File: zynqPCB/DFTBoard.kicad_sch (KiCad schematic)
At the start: 0 parts

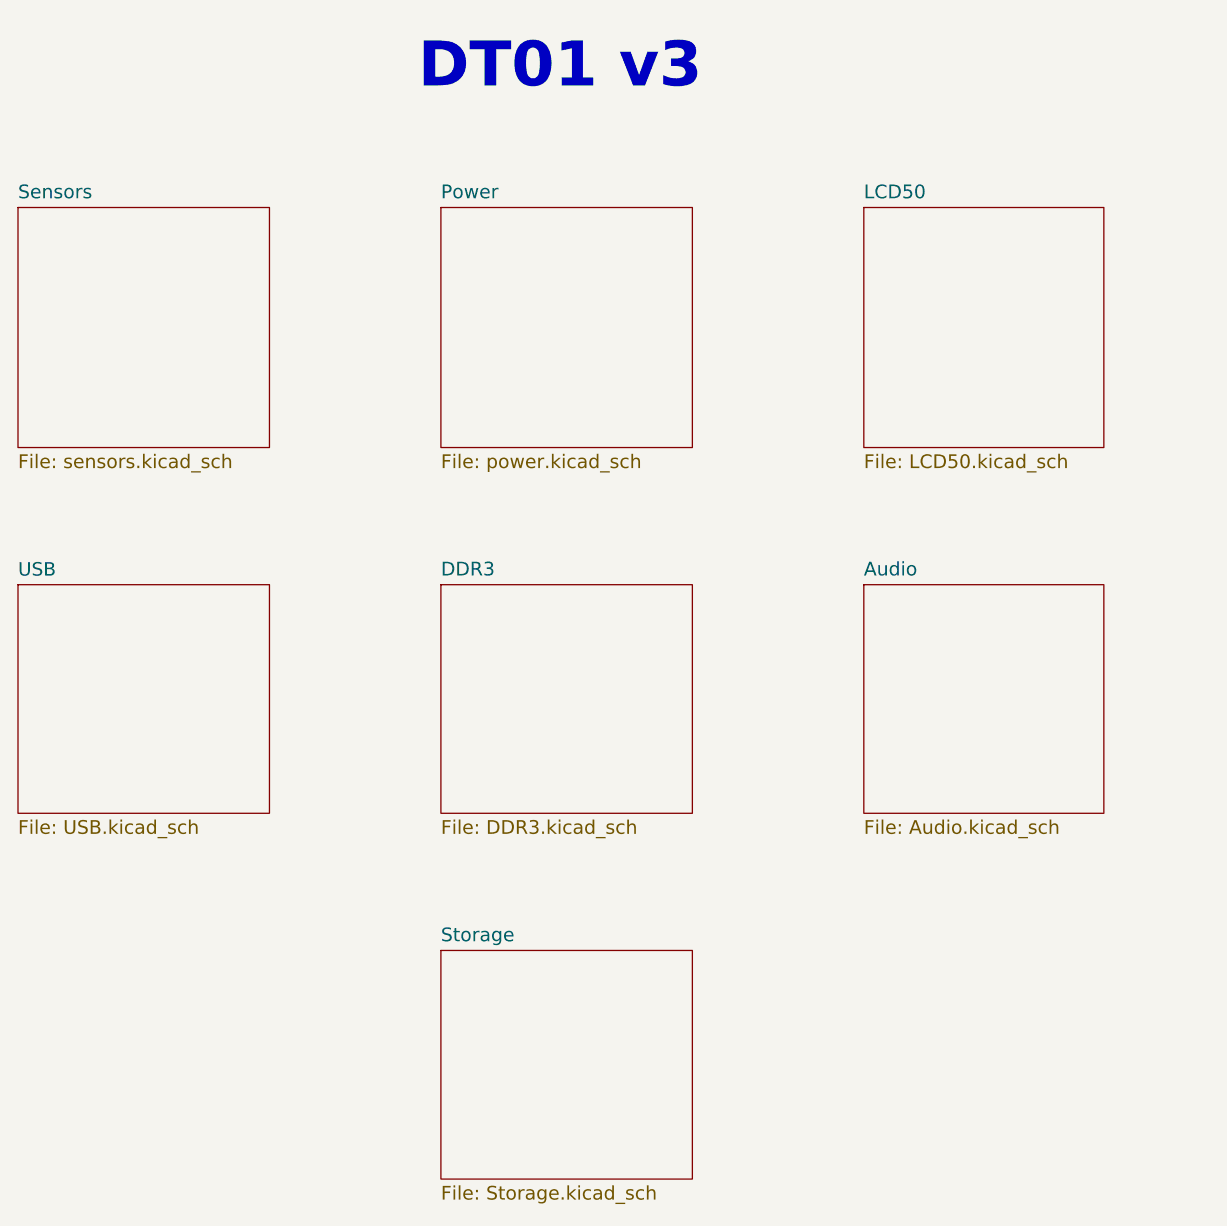
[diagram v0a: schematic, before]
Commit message: Sensores Removed
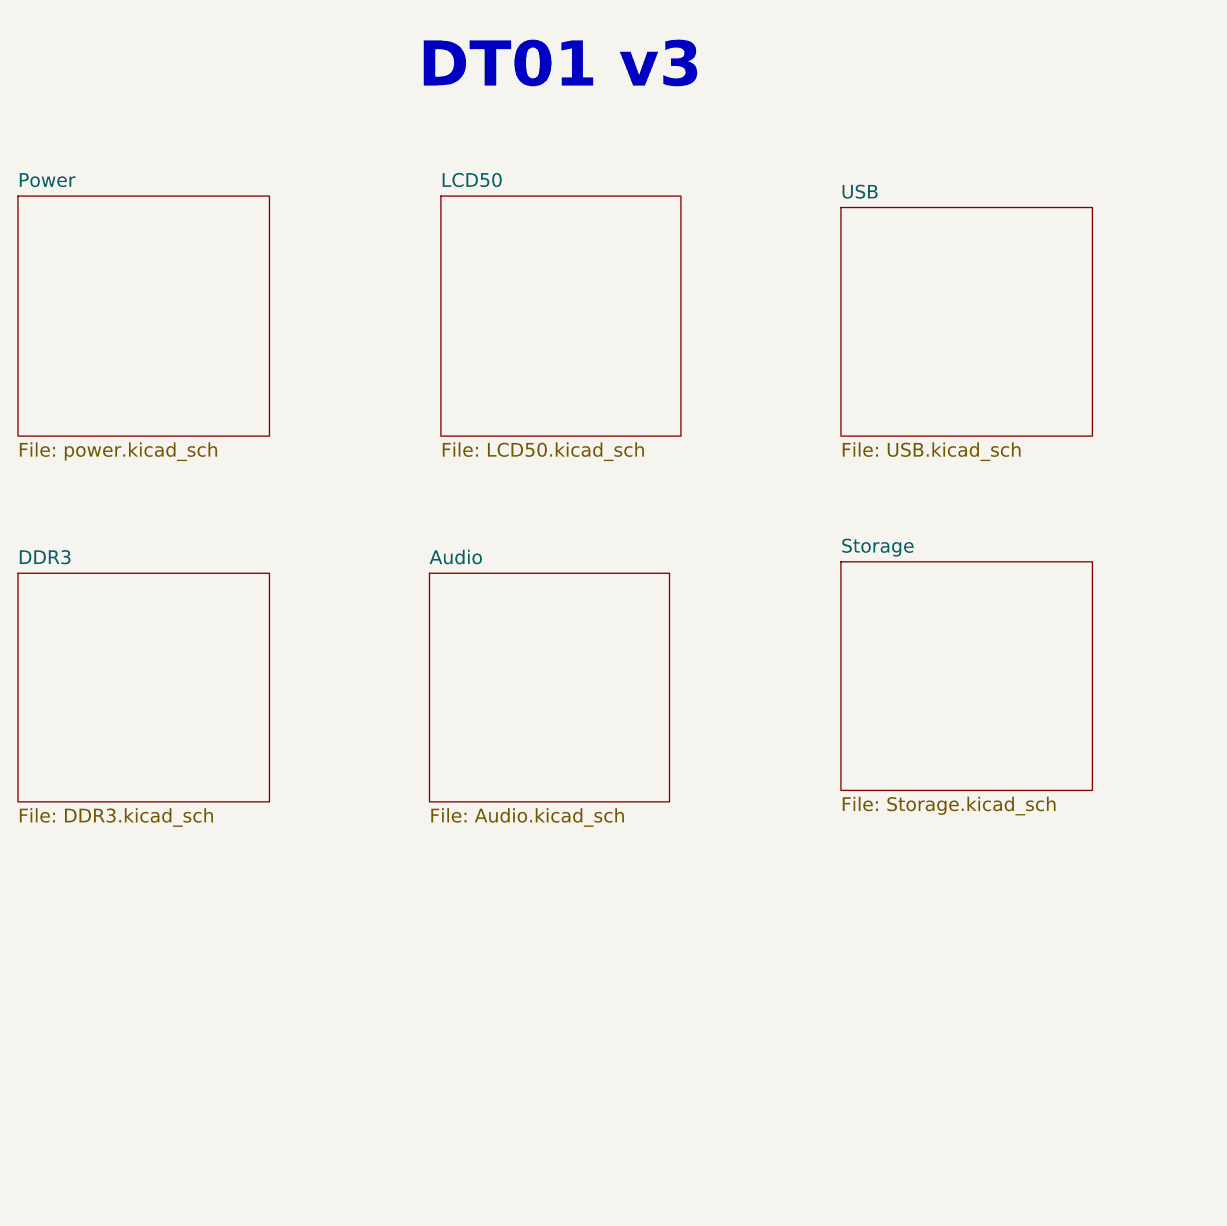
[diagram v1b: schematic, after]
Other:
- removed sheet Sensors
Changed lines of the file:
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@@
 	)
 	(sheet
-		(at 137.16 52.07)
+		(at 90.17 50.8)
 		(size 27.94 26.67)
 		(exclude_from_sim no)
@@
 		)
 		(property "Sheetname" "Power"
-			(at 137.16 51.2314 0)
+			(at 90.17 49.9614 0)
 			(effects
 				(font
@@
 		)
 		(property "Sheetfile" "power.kicad_sch"
-			(at 137.16 79.4262 0)
+			(at 90.17 78.1562 0)
 			(effects
 				(font
@@
 	)
 	(sheet
-		(at 184.15 93.98)
+		(at 135.89 92.71)
 		(size 26.67 25.4)
 		(exclude_from_sim no)
@@
 		)
 		(property "Sheetname" "Audio"
-			(at 184.15 93.1414 0)
+			(at 135.89 91.8714 0)
 			(effects
 				(font
@@
 		)
 		(property "Sheetfile" "Audio.kicad_sch"
-			(at 184.15 120.0662 0)
+			(at 135.89 118.7962 0)
 			(effects
 				(font
@@
 	)
 	(sheet
-		(at 90.17 93.98)
+		(at 181.61 52.07)
 		(size 27.94 25.4)
 		(exclude_from_sim no)
@@
 		)
 		(property "Sheetname" "USB"
-			(at 90.17 93.1541 0)
+			(at 181.61 51.2441 0)
 			(effects
 				(font
@@
 		)
 		(property "Sheetfile" "USB.kicad_sch"
-			(at 90.17 120.0662 0)
+			(at 181.61 78.1562 0)
 			(effects
 				(font
@@
 	)
 	(sheet
-		(at 90.17 52.07)
-		(size 27.94 26.67)
-		(exclude_from_sim no)
-		(in_bom yes)
-		(on_board yes)
-		(dnp no)
-		(fields_autoplaced yes)
-		(stroke
-			(width 0)
-			(type solid)
-		)
-		(fill
-			(color 0 0 0 0.0000)
-		)
-		(property "Sheetname" "Sensors"
-			(at 90.17 51.2314 0)
-			(effects
-				(font
-					(size 1.524 1.524)
-				)
-				(justify left bottom)
-			)
-		)
-		(property "Sheetfile" "sensors.kicad_sch"
-			(at 90.17 79.4262 0)
-			(effects
-				(font
-					(size 1.524 1.524)
-				)
-				(justify left top)
-			)
-		)
-		(instances
-			(project "DFTBoard"
-				(path "/49eba173-d38c-4d05-b21c-b4a14c4948c2"
-					(page "2")
-				)
-			)
-		)
-	)
-	(sheet
-		(at 137.16 93.98)
+		(at 90.17 92.71)
 		(size 27.94 25.4)
 		(exclude_from_sim no)
@@
 		)
 		(property "Sheetname" "DDR3"
-			(at 137.16 93.1414 0)
+			(at 90.17 91.8714 0)
 			(effects
 				(font
@@
 		)
 		(property "Sheetfile" "DDR3.kicad_sch"
-			(at 137.16 120.0662 0)
+			(at 90.17 118.7962 0)
 			(effects
 				(font
@@
 	)
 	(sheet
-		(at 184.15 52.07)
+		(at 137.16 50.8)
 		(size 26.67 26.67)
 		(exclude_from_sim no)
@@
 		)
 		(property "Sheetname" "LCD50"
-			(at 184.15 51.2314 0)
+			(at 137.16 49.9614 0)
 			(effects
 				(font
@@
 		)
 		(property "Sheetfile" "LCD50.kicad_sch"
-			(at 184.15 79.4262 0)
+			(at 137.16 78.1562 0)
 			(effects
 				(font
@@
 	)
 	(sheet
-		(at 137.16 134.62)
+		(at 181.61 91.44)
 		(size 27.94 25.4)
 		(exclude_from_sim no)
@@
 		)
 		(property "Sheetname" "Storage"
-			(at 137.16 133.7814 0)
+			(at 181.61 90.6014 0)
 			(effects
 				(font
@@
 		)
 		(property "Sheetfile" "Storage.kicad_sch"
-			(at 137.16 160.7062 0)
-			(effects
-				(font
+			(at 181.61 117.5262 0)
+			(effects
+				(font

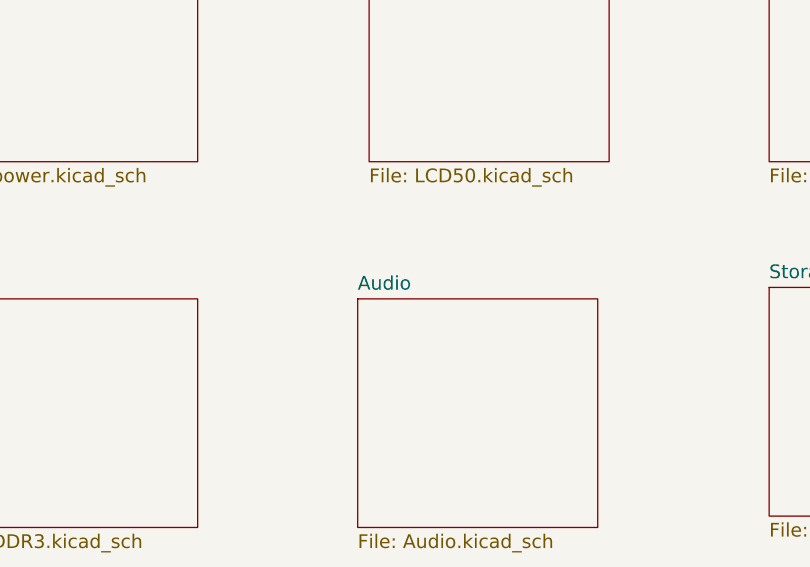
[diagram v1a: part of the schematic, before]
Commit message: Camera added
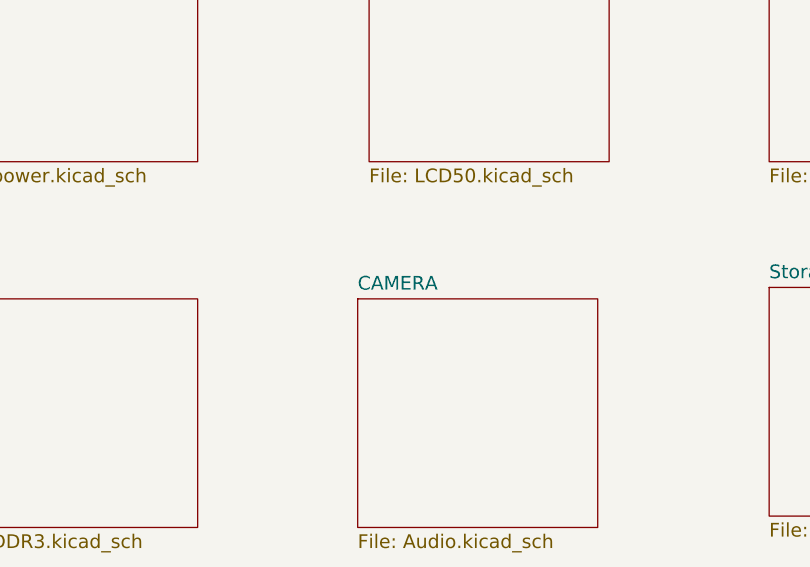
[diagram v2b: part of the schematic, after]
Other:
- sheet Audio renamed CAMERA
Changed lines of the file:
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@@
 (kicad_sch
-	(version 20250114)
+	(version 20260306)
 	(generator "eeschema")
-	(generator_version "9.0")
+	(generator_version "10.0")
 	(paper "A4")
 	(text "DT01 v3"
@@
 		)
 		(fill
-			(color 0 0 0 0.0000)
+			(color 0 0 0 0)
 		)
 		(property "Sheetname" "Power"
 			(at 90.17 49.9614 0)
+			(show_name no)
+			(do_not_autoplace no)
 			(effects
 				(font
@@
 		(property "Sheetfile" "power.kicad_sch"
 			(at 90.17 78.1562 0)
+			(show_name no)
+			(do_not_autoplace no)
 			(effects
 				(font
@@
 		)
 		(fill
-			(color 0 0 0 0.0000)
-		)
-		(property "Sheetname" "Audio"
+			(color 0 0 0 0)
+		)
+		(property "Sheetname" "CAMERA"
 			(at 135.89 91.8714 0)
+			(show_name no)
+			(do_not_autoplace no)
 			(effects
 				(font
@@
 		(property "Sheetfile" "Audio.kicad_sch"
 			(at 135.89 118.7962 0)
+			(show_name no)
+			(do_not_autoplace no)
 			(effects
 				(font
@@
 		)
 		(fill
-			(color 0 0 0 0.0000)
+			(color 0 0 0 0)
 		)
 		(property "Sheetname" "USB"
 			(at 181.61 51.2441 0)
+			(show_name no)
+			(do_not_autoplace no)
 			(effects
 				(font
@@
 		(property "Sheetfile" "USB.kicad_sch"
 			(at 181.61 78.1562 0)
+			(show_name no)
+			(do_not_autoplace no)
 			(effects
 				(font
@@
 		)
 		(fill
-			(color 0 0 0 0.0000)
+			(color 0 0 0 0)
 		)
 		(property "Sheetname" "DDR3"
 			(at 90.17 91.8714 0)
+			(show_name no)
+			(do_not_autoplace no)
 			(effects
 				(font
@@
 		(property "Sheetfile" "DDR3.kicad_sch"
 			(at 90.17 118.7962 0)
+			(show_name no)
+			(do_not_autoplace no)
 			(effects
 				(font
@@
 		)
 		(fill
-			(color 0 0 0 0.0000)
+			(color 0 0 0 0)
 		)
 		(property "Sheetname" "LCD50"
 			(at 137.16 49.9614 0)
+			(show_name no)
+			(do_not_autoplace no)
 			(effects
 				(font
@@
 		(property "Sheetfile" "LCD50.kicad_sch"
 			(at 137.16 78.1562 0)
+			(show_name no)
+			(do_not_autoplace no)
 			(effects
 				(font
@@
 		)
 		(fill
-			(color 0 0 0 0.0000)
+			(color 0 0 0 0)
 		)
 		(property "Sheetname" "Storage"
 			(at 181.61 90.6014 0)
+			(show_name no)
+			(do_not_autoplace no)
 			(effects
 				(font
@@
 		(property "Sheetfile" "Storage.kicad_sch"
 			(at 181.61 117.5262 0)
-			(effects
-				(font
+			(show_name no)
+			(do_not_autoplace no)
+			(effects
+				(font

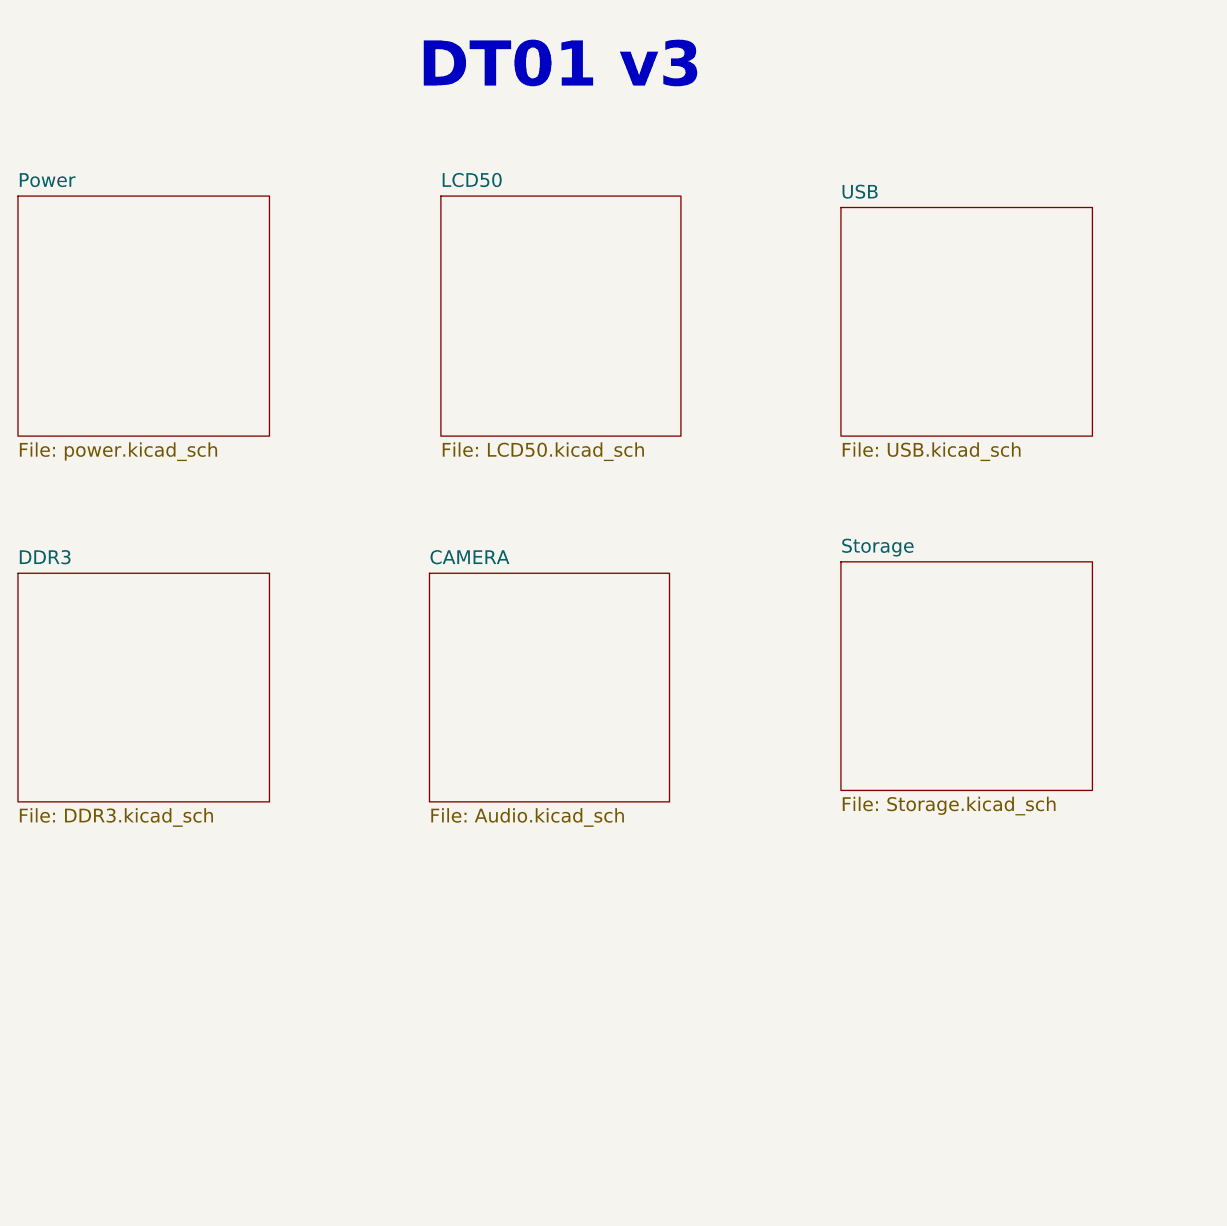
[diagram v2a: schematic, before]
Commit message: Cleared ERC error except the sequencer Part
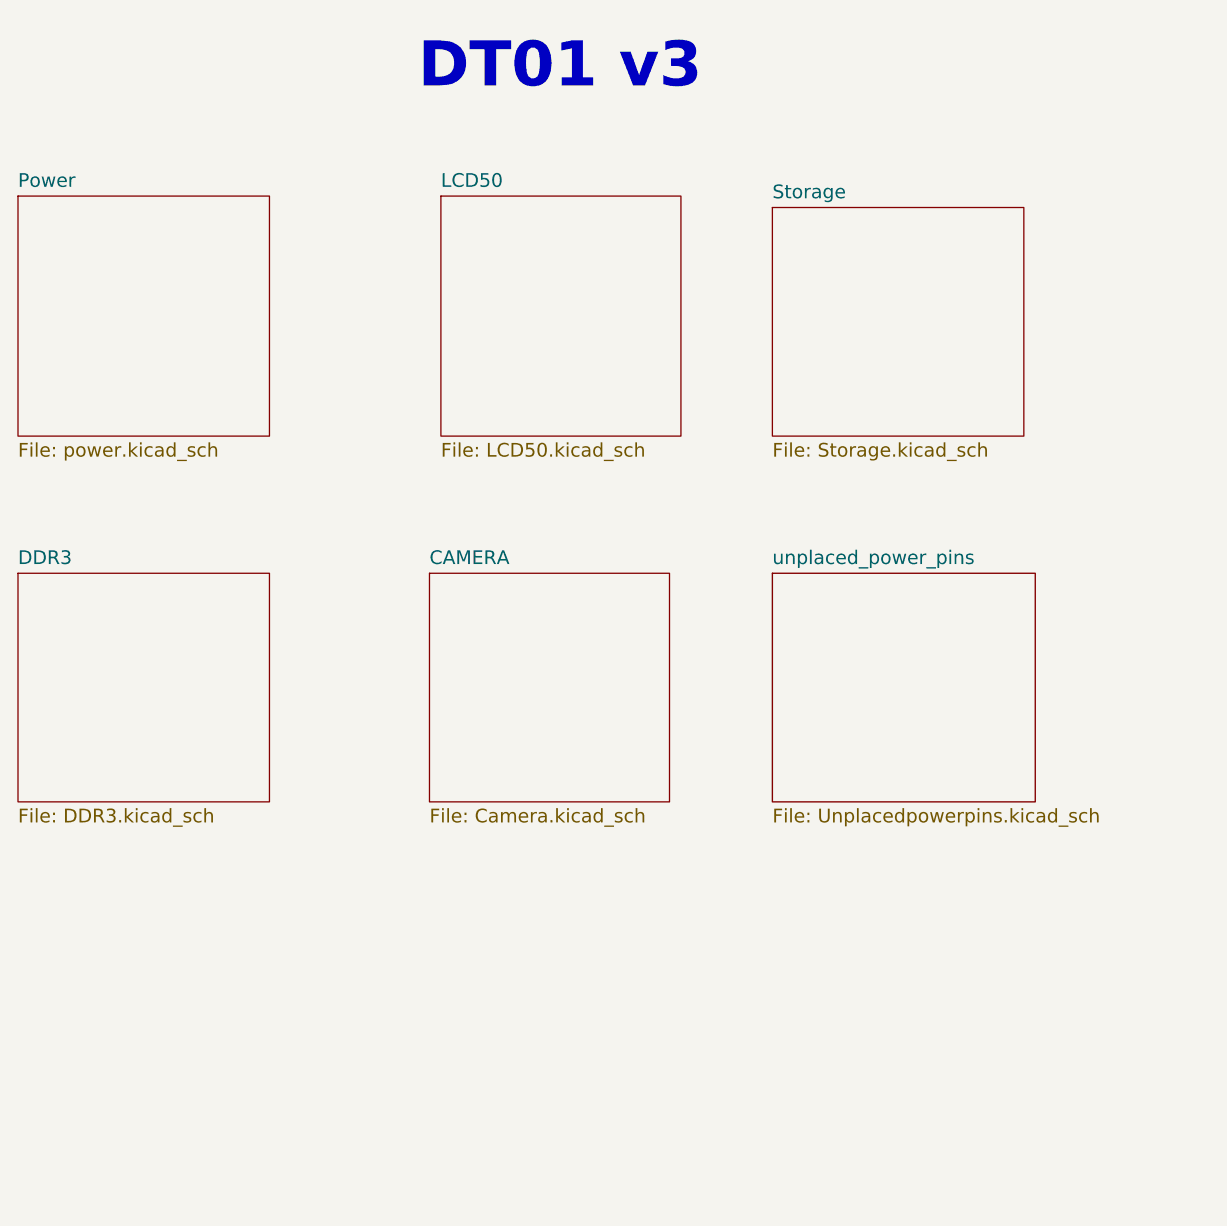
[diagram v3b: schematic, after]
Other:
- removed sheet USB
- added sheet unplaced_power_pins (Unplacedpowerpins.kicad_sch)
- sheet CAMERA: file Audio.kicad_sch -> Camera.kicad_sch
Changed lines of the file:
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@@
 	(generator_version "10.0")
 	(paper "A4")
+	(rectangle
+		(start 182.88 105.41)
+		(end 182.88 105.41)
+		(stroke
+			(width 0)
+			(type default)
+		)
+		(fill
+			(type none)
+		)
+	)
 	(text "DT01 v3"
 		(exclude_from_sim no)
@@
 			)
 		)
-		(property "Sheetfile" "Audio.kicad_sch"
+		(property "Sheetfile" "Camera.kicad_sch"
 			(at 135.89 118.7962 0)
 			(show_name no)
@@
 				(path "/49eba173-d38c-4d05-b21c-b4a14c4948c2"
 					(page "8")
-				)
-			)
-		)
-	)
-	(sheet
-		(at 181.61 52.07)
-		(size 27.94 25.4)
-		(exclude_from_sim no)
-		(in_bom yes)
-		(on_board yes)
-		(dnp no)
-		(fields_autoplaced yes)
-		(stroke
-			(width 0)
-			(type solid)
-		)
-		(fill
-			(color 0 0 0 0)
-		)
-		(property "Sheetname" "USB"
-			(at 181.61 51.2441 0)
-			(show_name no)
-			(do_not_autoplace no)
-			(effects
-				(font
-					(size 1.4986 1.4986)
-				)
-				(justify left bottom)
-			)
-		)
-		(property "Sheetfile" "USB.kicad_sch"
-			(at 181.61 78.1562 0)
-			(show_name no)
-			(do_not_autoplace no)
-			(effects
-				(font
-					(size 1.524 1.524)
-				)
-				(justify left top)
-			)
-		)
-		(instances
-			(project "DFTBoard"
-				(path "/49eba173-d38c-4d05-b21c-b4a14c4948c2"
-					(page "3")
 				)
 			)
@@
 	)
 	(sheet
-		(at 181.61 91.44)
+		(at 173.99 52.07)
 		(size 27.94 25.4)
 		(exclude_from_sim no)
@@
 		)
 		(property "Sheetname" "Storage"
-			(at 181.61 90.6014 0)
+			(at 173.99 51.2314 0)
 			(show_name no)
 			(do_not_autoplace no)
@@
 		)
 		(property "Sheetfile" "Storage.kicad_sch"
-			(at 181.61 117.5262 0)
+			(at 173.99 78.1562 0)
 			(show_name no)
 			(do_not_autoplace no)
@@
 				)
 			)
+		)
+	)
+	(sheet
+		(at 173.99 92.71)
+		(size 29.21 25.4)
+		(exclude_from_sim no)
+		(in_bom yes)
+		(on_board yes)
+		(dnp no)
+		(fields_autoplaced yes)
+		(stroke
+			(width 0.1524)
+			(type solid)
+		)
+		(fill
+			(color 0 0 0 0)
+		)
+		(property "Sheetname" "unplaced_power_pins"
+			(at 173.99 91.8714 0)
+			(show_name no)
+			(do_not_autoplace no)
+			(effects
+				(font
+					(size 1.524 1.524)
+				)
+				(justify left bottom)
+			)
+		)
+		(property "Sheetfile" "Unplacedpowerpins.kicad_sch"
+			(at 173.99 118.7962 0)
+			(show_name no)
+			(do_not_autoplace no)
+			(effects
+				(font
+					(size 1.524 1.524)
+				)
+				(justify left top)
+			)
+		)
+		(instances
+			(project "DFTBoard"
+				(path "/49eba173-d38c-4d05-b21c-b4a14c4948c2"
+					(page "2")
+				)
+			)

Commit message: Sequencing is taken care
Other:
- removed sheet unplaced_power_pins
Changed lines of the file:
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@@
-		)
-	)
-	(sheet
-		(at 173.99 92.71)
-		(size 29.21 25.4)
-		(exclude_from_sim no)
-		(in_bom yes)
-		(on_board yes)
-		(dnp no)
-		(fields_autoplaced yes)
-		(stroke
-			(width 0.1524)
-			(type solid)
-		)
-		(fill
-			(color 0 0 0 0)
-		)
-		(property "Sheetname" "unplaced_power_pins"
-			(at 173.99 91.8714 0)
-			(show_name no)
-			(do_not_autoplace no)
-			(effects
-				(font
-					(size 1.524 1.524)
-				)
-				(justify left bottom)
-			)
-		)
-		(property "Sheetfile" "Unplacedpowerpins.kicad_sch"
-			(at 173.99 118.7962 0)
-			(show_name no)
-			(do_not_autoplace no)
-			(effects
-				(font
-					(size 1.524 1.524)
-				)
-				(justify left top)
-			)
-		)
-		(instances
-			(project "DFTBoard"
-				(path "/49eba173-d38c-4d05-b21c-b4a14c4948c2"
-					(page "2")
-				)
-			)
 		)
 	)
